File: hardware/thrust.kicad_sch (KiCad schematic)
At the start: 42 parts, among them J18 LUG BATT+, J19 LUG MOTOR A, J20 LUG MOTOR B, J21 LUG GND, Q10 IRF100P219, Q3 IRF100P219, Q4 IRF100P219, Q5 IRF100P219, Q6 IRF100P219, Q7 IRF100P219, Q8 IRF100P219, Q9 IRF100P219, U10 ACS758LCB-100B, U9 HIP4082IPZ

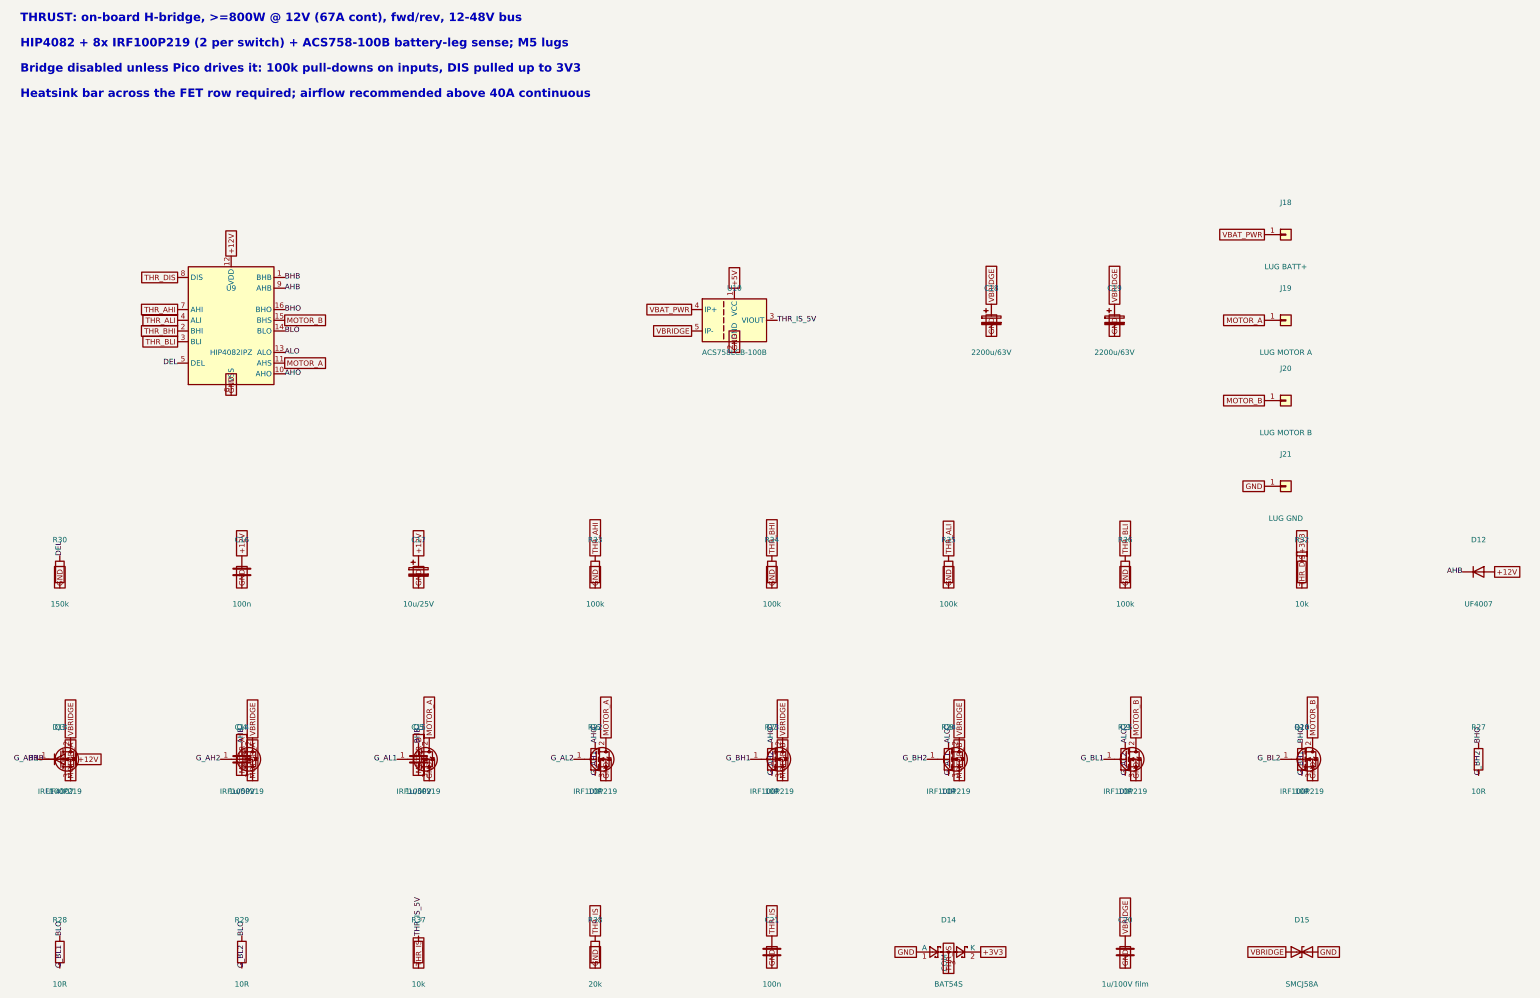
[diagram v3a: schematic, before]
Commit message: cost pass 10 (schematic): remove on-board H-bridge, add J13 external-driver header (IBT-2 pinout); ERC 0, gate PASS
Co-Authored-By: Claude Fable 5 <noreply@anthropic.com>
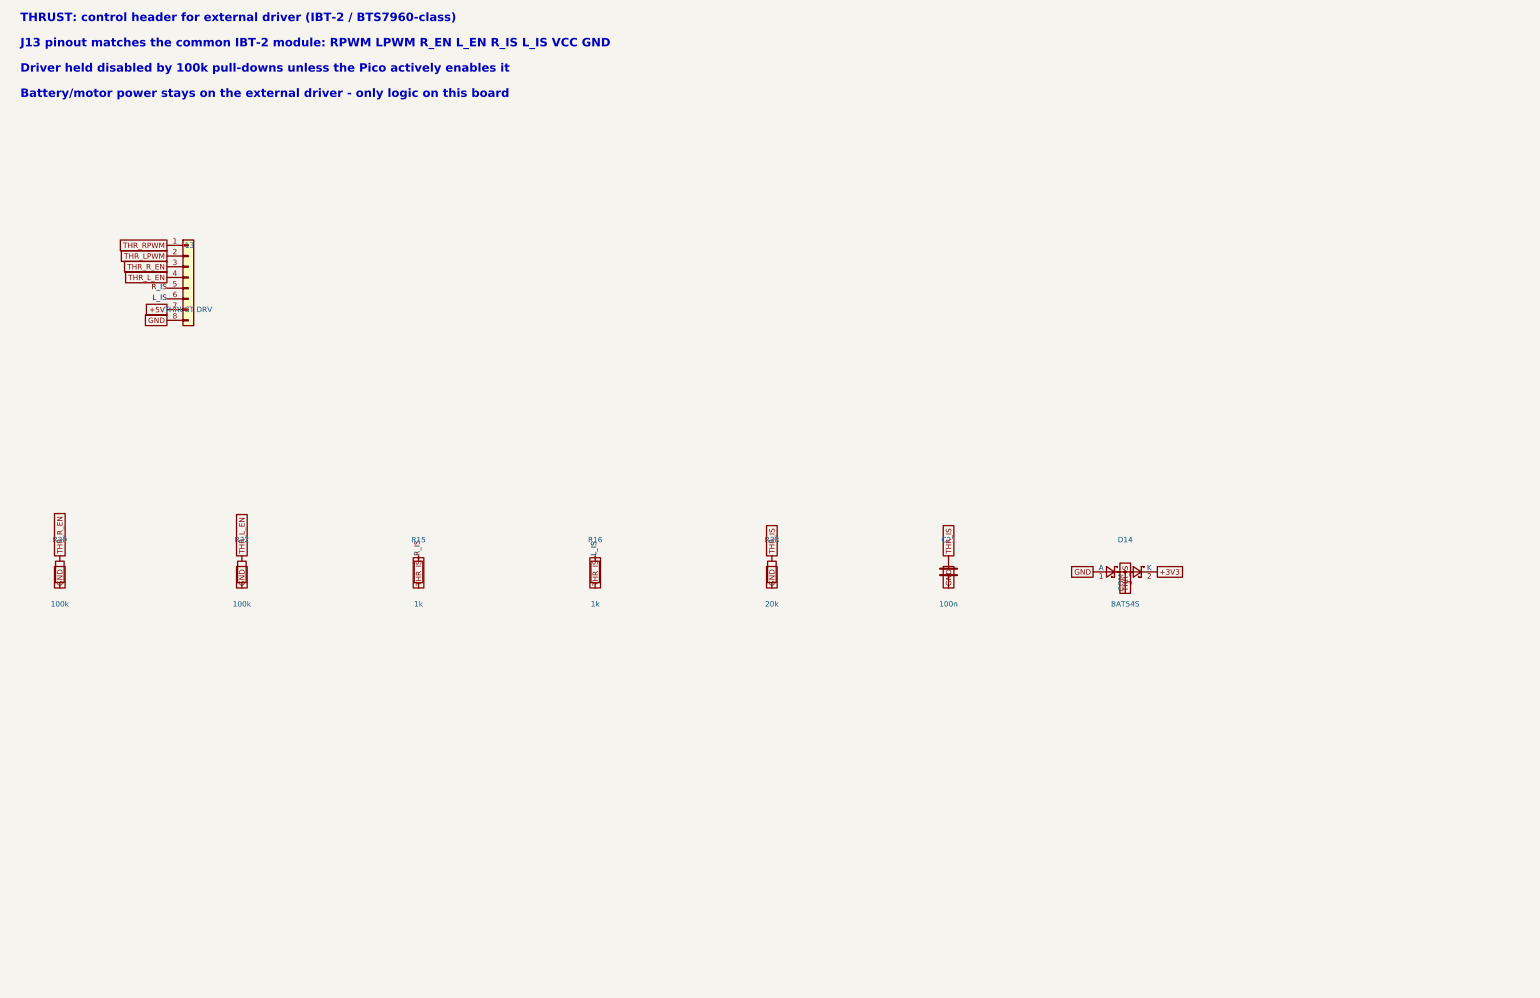
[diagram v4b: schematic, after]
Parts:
- removed C14, C15: 1u/50V, Capacitor_THT:C_Disc_D5.0mm_W2.5mm_P5.00mm, symbol Device:C
- removed C16: 100n, Capacitor_THT:C_Disc_D5.0mm_W2.5mm_P5.00mm, symbol Device:C
- removed C17: 10u/25V, Capacitor_THT:CP_Radial_D5.0mm_P2.00mm, symbol Device:C_Polarized
- removed C18, C19: 2200u/63V, Capacitor_THT:CP_Radial_D18.0mm_P7.50mm, symbol Device:C_Polarized
- removed C20: 1u/100V film, Capacitor_THT:C_Disc_D5.0mm_W2.5mm_P5.00mm, symbol Device:C
- removed D12, D13: UF4007, Diode_THT:D_DO-41_SOD81_P10.16mm_Horizontal, symbol Diode:1N4007
- removed D15: SMCJ58A, Diode_SMD:D_SMC, symbol Device:D_TVS
- removed J18: LUG BATT+, vanchor-helm:Lug_M5, symbol Connector_Generic:Conn_01x01
- removed J19: LUG MOTOR A, vanchor-helm:Lug_M5, symbol Connector_Generic:Conn_01x01
- removed J20: LUG MOTOR B, vanchor-helm:Lug_M5, symbol Connector_Generic:Conn_01x01
- removed J21: LUG GND, vanchor-helm:Lug_M5, symbol Connector_Generic:Conn_01x01
- removed Q10, Q3, Q4, Q5, Q6, Q7, Q8, Q9: IRF100P219, Package_TO_SOT_THT:TO-220-3_Vertical, symbol Transistor_FET:IRLZ44N
- removed R22, R23, R24, R25, R26, R27, R28, R29: 10R, Resistor_THT:R_Axial_DIN0207_L6.3mm_D2.5mm_P2.54mm_Vertical, symbol Device:R
- removed R33, R34, R35, R36: 100k, Resistor_THT:R_Axial_DIN0207_L6.3mm_D2.5mm_P10.16mm_Horizontal, symbol Device:R
- removed R37: 10k, Resistor_THT:R_Axial_DIN0207_L6.3mm_D2.5mm_P10.16mm_Horizontal, symbol Device:R
- removed U10: ACS758LCB-100B, Sensor_Current:Allegro_CB_PFF, symbol Sensor_Current:ACS758xCB-100B-PFF
- removed U9: HIP4082IPZ, Package_DIP:DIP-16_W7.62mm_Socket, symbol Driver_FET:HIP4082xP
- added J13: THRUST DRV, Connector_PinHeader_2.54mm:PinHeader_1x08_P2.54mm_Vertical, symbol Connector_Generic:Conn_01x08
- added R15, R16: 1k, Resistor_THT:R_Axial_DIN0207_L6.3mm_D2.5mm_P10.16mm_Horizontal, symbol Device:R
- R30: value 150k -> 100k
- R32: value 10k -> 100k
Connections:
- net THR_DIS is gone; now on net GND: R32.2
- net +3V3: no longer R32.1
- net +5V: now also J13.7 (Pin_7)
- net GND: now also J13.8 (Pin_8)
- net THR_IS: now also R15.2, R16.2
- net DEL renamed THR_R_EN
- net THR_R_EN: now also J13.3 (Pin_3)
- new net L_IS: J13.6 (Pin_6), R16.1
- new net R_IS: J13.5 (Pin_5), R15.1
- new net THR_LPWM: J13.2 (Pin_2)
- new net THR_L_EN: J13.4 (Pin_4), R32.1
- new net THR_RPWM: J13.1 (Pin_1)
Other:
- note added: "Battery/motor power stays on the external driver - only logic on this board"
- note added: "Driver held disabled by 100k pull-downs unless the Pico actively enables it"
- note added: "J13 pinout matches the common IBT-2 module: RPWM LPWM R_EN L_EN R_IS L_IS VCC GND"
- note added: "THRUST: control header for external driver (IBT-2 / BTS7960-class)"
- note removed: "Bridge disabled unless Pico drives it: 100k pull-downs on inputs, DIS pulled up to 3V3"
- note removed: "HIP4082 + 8x IRF100P219 (2 per switch) + ACS758-100B battery-leg sense; M5 lugs"
- note removed: "Heatsink bar across the FET row required; airflow recommended above 40A continuous"
- note removed: "THRUST: on-board H-bridge, >=800W @ 12V (67A cont), fwd/rev, 12-48V bus"
- moved on the sheet: C21, D14, R32, R38
